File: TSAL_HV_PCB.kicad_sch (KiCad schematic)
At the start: 36 parts, among them J3 Conn_01x03_Socket, J4 Conn_01x03_Socket, K1 SPU01M-12, U1 LM393, U2 4N35, U3 TPS7B88-Q1

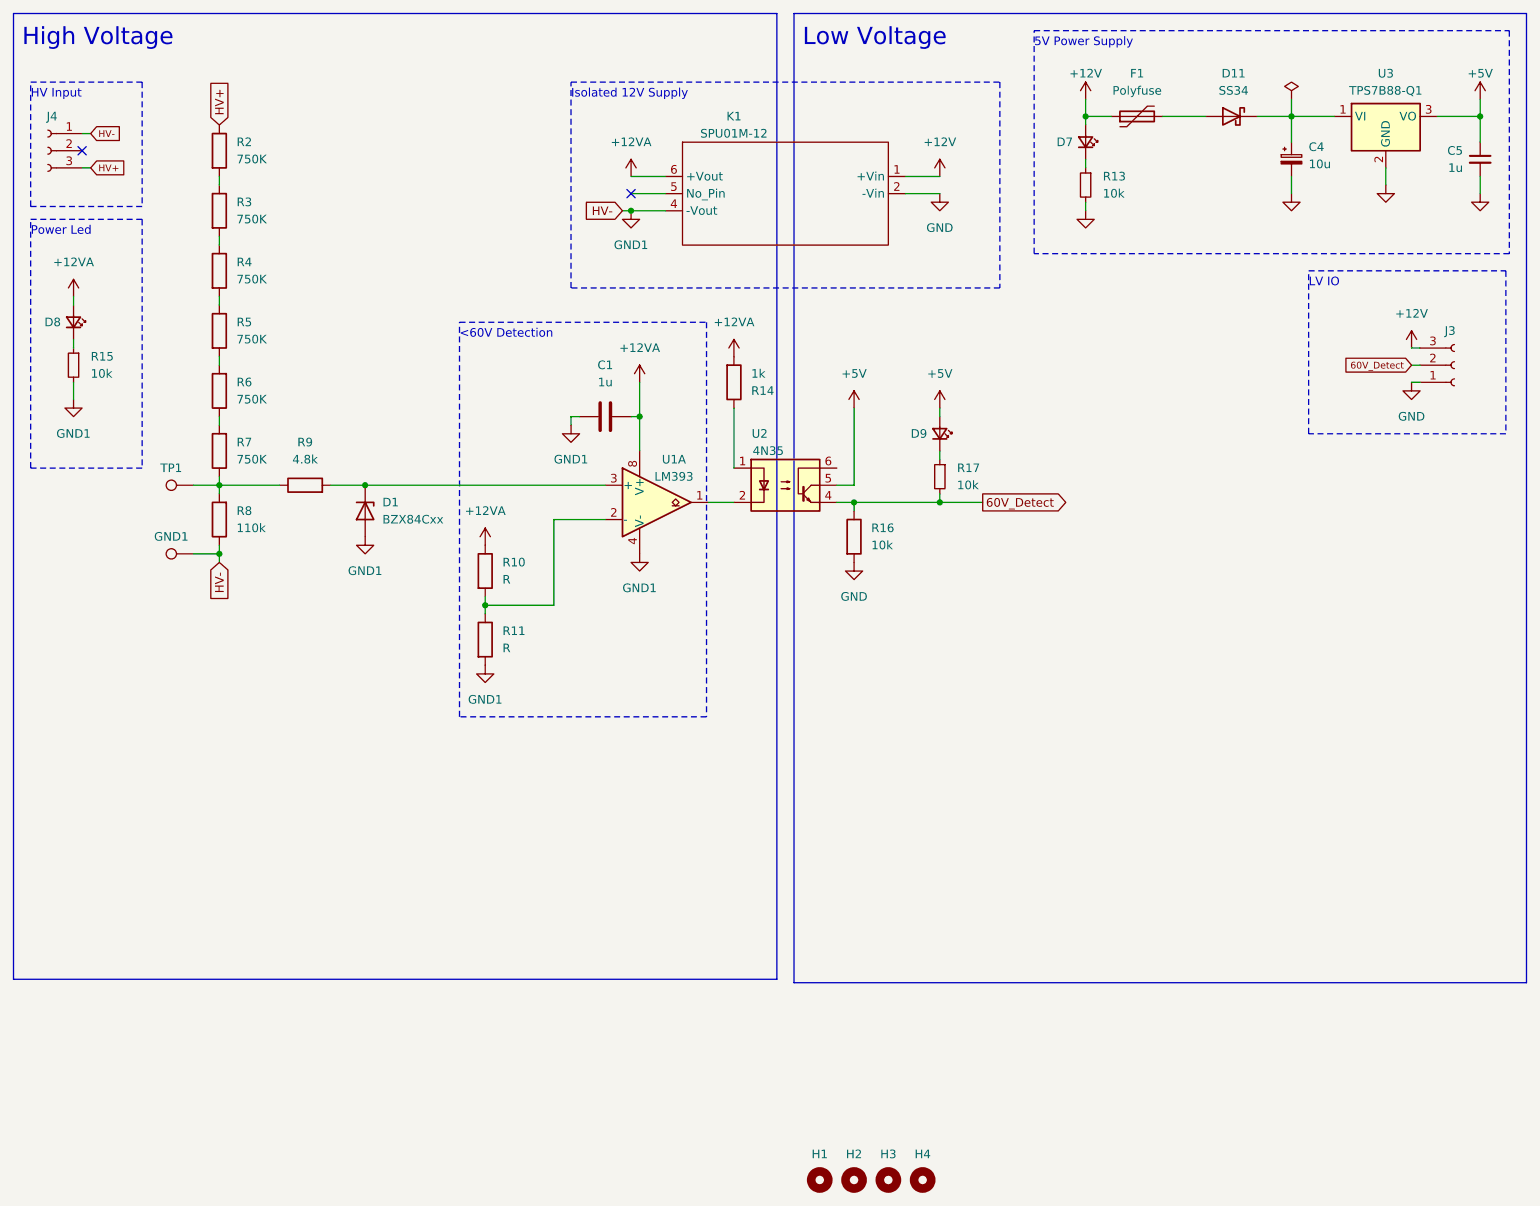
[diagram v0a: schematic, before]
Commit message: Changed LED Indicator, updated footprints
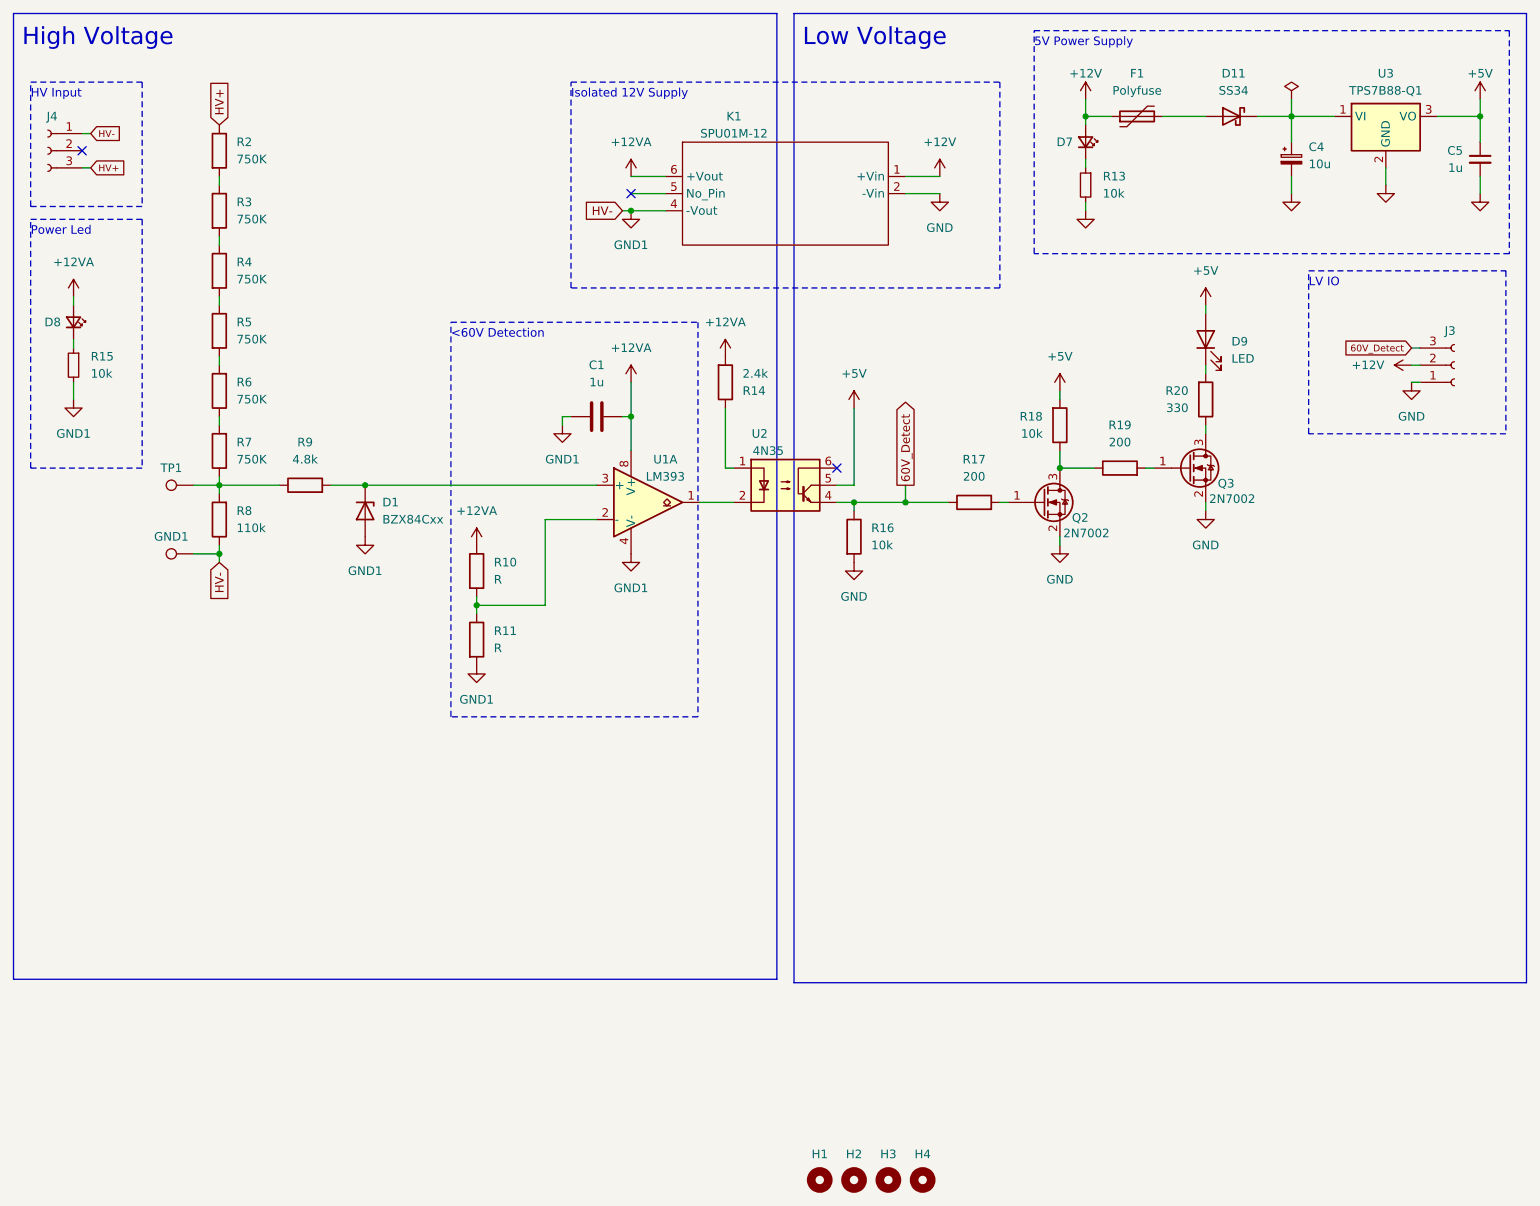
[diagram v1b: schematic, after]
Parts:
- removed D9: LED_Small, LED_SMD:LED_0603_1608Metric, symbol Device:LED_Small
- removed R17: 10k, Resistor_SMD:R_0603_1608Metric, symbol Device:R_Small
- added D9: LED, LED_SMD:LED_0603_1608Metric, symbol Device:LED
- added Q2, Q3: 2N7002, Package_TO_SOT_SMD:SOT-23, symbol Transistor_FET:2N7002
- added R17, R19: 200, Resistor_SMD:R_0603_1608Metric, symbol Device:R
- added R18: 10k, Resistor_SMD:R_0603_1608Metric, symbol Device:R
- added R20: 330, Resistor_SMD:R_0603_1608Metric, symbol Device:R
- J3, J4: footprint MyLibrary:MolexMicrofitPlus1x3 -> yfs:MolexMicrofitPlus1x3
- K1: footprint MyLibrary:SPU01M-12 -> yfs:SPU01M-12
- R14: value 1k -> 2.4k
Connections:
- net +12V: now also J3.2 (Pin_2); no longer J3.3 (Pin_3)
- net +5V: now also D9.2 (A), R18.2
- net 60V_Detect: now also J3.3 (Pin_3), R17.1; no longer J3.2 (Pin_2)
- net GND: now also Q2.2 (S), Q3.2 (S)
- new net: Q2.3 (D), R18.1, R19.1
- new net: Q3.1 (G), R19.2
- new net: Q3.3 (D), R20.1
- new net: Q2.1 (G), R17.2
- new net: D9.1 (K), R20.2
- no-connect marks 2 -> 3
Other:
- moved on the sheet: C1, R10, R11, R14, U1A

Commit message: Changed DC-DC Converter
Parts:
- removed D1: BZX84Cxx, Package_TO_SOT_SMD:SOT-23, symbol Diode:BZX84Cxx
- added D1: BZX384xxxx, Diode_SMD:D_SOD-323, symbol Diode:BZX384xxxx
- D11: value SS34 -> NSR0530HT1G; footprint Diode_SMD:D_SMA -> Diode_SMD:D_SOD-323
- K1: value SPU01M-12 -> SPU01M-5; footprint yfs:SPU01M-12 -> yfs:SPU01M-5
- R14: value 2.4k -> 1.8k
- R15: value 10k -> 1k
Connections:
- net GND1: now also D1.2 (A)
- net at R9.2, U1.3 (+): now also D1.1 (K)
- net +12VA renamed +5VA
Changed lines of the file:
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@@
 	)
 	(junction
-		(at 86.36 87.63)
-		(diameter 0)
-		(color 0 0 0 0)
-	)
-	(junction
 		(at 166.37 90.17)
 		(diameter 0)
@@
 		(color 0 0 0 0)
 	)
+	(junction
+		(at 86.36 87.63)
+		(diameter 0)
+		(color 0 0 0 0)
+	)
 	(no_connect
 		(at 44.45 38.1)
@@
 	(wire
 		(pts
+			(xy 86.36 87.63) (xy 120.65 87.63)
+		)
+		(stroke
+			(width 0)
+			(type default)
+		)
+	)
+	(wire
+		(pts
 			(xy 210.82 90.17) (xy 210.82 91.44)
 		)
@@
 	(wire
 		(pts
-			(xy 86.36 87.63) (xy 120.65 87.63)
-		)
-		(stroke
-			(width 0)
-			(type default)
-		)
-	)
-	(wire
-		(pts
 			(xy 210.82 60.96) (xy 210.82 62.23)
 		)
@@
 	)
 	(symbol
-		(lib_id "Diode:BZX84Cxx")
-		(at 86.36 91.44 270)
-		(unit 1)
-		(exclude_from_sim no)
-		(in_bom yes)
-		(on_board yes)
-		(dnp no)
-		(fields_autoplaced yes)
-		(property "Reference" "D1"
-			(at 88.9 90.17 90)
-			(effects
-				(font
-					(size 1.27 1.27)
-				)
-				(justify left)
-			)
-		)
-		(property "Value" "BZX84Cxx"
-			(at 88.9 92.71 90)
-			(effects
-				(font
-					(size 1.27 1.27)
-				)
-				(justify left)
-			)
-		)
-		(property "Footprint" "Package_TO_SOT_SMD:SOT-23"
-			(at 86.36 91.44 0)
-			(effects
-				(font
-					(size 1.27 1.27)
-				)
-				(hide yes)
-			)
-		)
-		(property "Datasheet" "https://diotec.com/tl_files/diotec/files/pdf/datasheets/bzx84c2v4.pdf"
-			(at 86.36 91.44 0)
-			(effects
-				(font
-					(size 1.27 1.27)
-				)
-				(hide yes)
-			)
-		)
-		(property "Description" ""
-			(at 86.36 91.44 0)
-			(effects
-				(font
-					(size 1.27 1.27)
-				)
-				(hide yes)
-			)
-		)
-		(pin "1"
-		)
-		(pin "2"
-		)
-		(pin "3"
-		)
-		(instances
-			(project "TSAL_HV_PCB"
-				(path "/49aa962b-9fa6-407b-842a-3cf8300a05dc"
-					(reference "D1")
-					(unit 1)
-				)
-			)
-		)
-	)
-	(symbol
 		(lib_id "power:+5V")
 		(at 189.23 73.66 0)
@@
 		(on_board yes)
 		(dnp no)
-		(fields_autoplaced yes)
 		(property "Reference" "#PWR09"
 			(at 125.73 45.72 0)
@@
 			)
 		)
-		(property "Value" "+12VA"
-			(at 125.73 36.83 0)
+		(property "Value" "+5VA"
+			(at 123.19 36.83 0)
 			(effects
 				(font
 					(size 1.27 1.27)
 				)
+				(justify left)
 			)
 		)
@@
 	)
 	(symbol
+		(lib_id "Diode:BZX384xxxx")
+		(at 86.36 91.44 270)
+		(unit 1)
+		(exclude_from_sim no)
+		(in_bom yes)
+		(on_board yes)
+		(dnp no)
+		(fields_autoplaced yes)
+		(property "Reference" "D1"
+			(at 88.9 90.1699 90)
+			(effects
+				(font
+					(size 1.27 1.27)
+				)
+				(justify left)
+			)
+		)
+		(property "Value" "BZX384xxxx"
+			(at 88.9 92.7099 90)
+			(effects
+				(font
+					(size 1.27 1.27)
+				)
+				(justify left)
+			)
+		)
+		(property "Footprint" "Diode_SMD:D_SOD-323"
+			(at 81.915 91.44 0)
+			(effects
+				(font
+					(size 1.27 1.27)
+				)
+				(hide yes)
+			)
+		)
+		(property "Datasheet" "https://www.vishay.com/docs/86474/bzx384.pdf"
+			(at 86.36 91.44 0)
+			(effects
+				(font
+					(size 1.27 1.27)
+				)
+				(hide yes)
+			)
+		)
+		(property "Description" "300mW Zener Diode, SOD-323"
+			(at 86.36 91.44 0)
+			(effects
+				(font
+					(size 1.27 1.27)
+				)
+				(hide yes)
+			)
+		)
+		(pin "2"
+		)
+		(pin "1"
+		)
+		(instances
+			(project "TSAL_HV_PCB"
+				(path "/49aa962b-9fa6-407b-842a-3cf8300a05dc"
+					(reference "D1")
+					(unit 1)
+				)
+			)
+		)
+	)
+	(symbol
 		(lib_id "power:GND")
 		(at 223.52 44.45 0)
@@
 		(on_board yes)
 		(dnp no)
-		(fields_autoplaced yes)
 		(property "Reference" "#PWR011"
 			(at 125.73 76.2 0)
@@
 			)
 		)
-		(property "Value" "+12VA"
-			(at 125.73 67.31 0)
+		(property "Value" "+5VA"
+			(at 123.19 68.58 0)
 			(effects
 				(font
 					(size 1.27 1.27)
 				)
+				(justify left)
 			)
 		)
@@
 			)
 		)
-		(property "Value" "10k"
+		(property "Value" "1k"
 			(at 45.72 71.1199 0)
 			(effects
@@
 			)
 		)
-		(property "Value" "+12VA"
+		(property "Value" "+5VA"
 			(at 43.18 54.61 0)
 			(effects
@@
 			)
 		)
-		(property "Value" "2.4k"
+		(property "Value" "1.8k"
 			(at 142.24 71.12 0)
 			(effects
@@
 			)
 		)
-		(property "Value" "SPU01M-12"
+		(property "Value" "SPU01M-5"
 			(at 140.97 35.56 0)
 			(effects
@@
 			)
 		)
-		(property "Footprint" "yfs:SPU01M-12"
+		(property "Footprint" "yfs:SPU01M-5"
 			(at 137.16 38.1 0)
 			(effects
@@
 			)
 		)
-		(property "Datasheet" ""
+		(property "Datasheet" "https://www.meanwellusa.com/webapp/product/search.aspx?prod=SPU01"
 			(at 137.16 38.1 0)
 			(effects
@@
 			)
 		)
-		(property "Description" ""
+		(property "Description" "Isolated DC/DC Converters - Through Hole 10.8-13.2Vin 5Vout 200mA SIP6 Unreg Iso"
 			(at 138.43 38.1 0)
 			(effects
@@
 			)
 		)
-		(property "Value" "SS34"
+		(property "Value" "NSR0530HT1G"
 			(at 214.9475 29.21 0)
 			(effects
@@
 			)
 		)
-		(property "Footprint" "Diode_SMD:D_SMA"
+		(property "Footprint" "Diode_SMD:D_SOD-323"
 			(at 214.63 37.465 0)
 			(effects
@@
 			)
 		)
-		(property "Datasheet" "https://www.vishay.com/docs/88751/ss32.pdf"
+		(property "Datasheet" "https://www.mouser.co.uk/datasheet/3/101/1/NSR0530H-D.PDF"
 			(at 214.63 33.02 0)
 			(effects
@@
 			)
 		)
-		(property "Description" "40V 3A Schottky Diode, SMA"
+		(property "Description" "Schottky Diodes & Rectifiers 0.5 A 30 V SOD-323 S"
 			(at 214.63 33.02 0)
 			(effects
@@
 			)
 		)
-		(property "Value" "+12VA"
+		(property "Value" "+5VA"
 			(at 102.87 91.44 0)
 			(effects
@@
 		(on_board yes)
 		(dnp no)
-		(fields_autoplaced yes)
 		(property "Reference" "#PWR013"
 			(at 139.7 72.39 0)
@@
 			)
 		)
-		(property "Value" "+12VA"
-			(at 139.7 63.5 0)
+		(property "Value" "+5VA"
+			(at 138.43 63.5 0)
 			(effects
 				(font
 					(size 1.27 1.27)
 				)
+				(justify left)
 			)
 		)

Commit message: Polyfuse for DC-DC supply
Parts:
- added F2: 500mA, Resistor_SMD:R_0805_2012Metric, symbol Device:Polyfuse
- F1: value Polyfuse -> 100mA
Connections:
- net +12V: now also F2.2; no longer K1.1 (+Vin)
- new net: F2.1, K1.1 (+Vin)
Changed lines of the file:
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@@
 	(rectangle
 		(start 116.84 27.94)
-		(end 180.34 58.42)
+		(end 182.88 58.42)
 		(stroke
 			(width 0)
@@
 	(wire
 		(pts
-			(xy 166.37 41.91) (xy 171.45 41.91)
+			(xy 201.93 85.09) (xy 203.2 85.09)
 		)
 		(stroke
@@
 	(wire
 		(pts
-			(xy 201.93 85.09) (xy 203.2 85.09)
+			(xy 241.3 72.39) (xy 242.57 72.39)
 		)
 		(stroke
@@
 	(wire
 		(pts
-			(xy 241.3 72.39) (xy 242.57 72.39)
+			(xy 193.04 30.48) (xy 193.04 33.02)
 		)
 		(stroke
@@
 	(wire
 		(pts
-			(xy 193.04 30.48) (xy 193.04 33.02)
+			(xy 172.72 41.91) (xy 166.37 41.91)
 		)
 		(stroke
@@
 	(symbol
 		(lib_id "power:+12V")
-		(at 171.45 41.91 0)
+		(at 172.72 34.29 0)
 		(unit 1)
 		(exclude_from_sim no)
@@
 		(fields_autoplaced yes)
 		(property "Reference" "#PWR019"
-			(at 171.45 45.72 0)
+			(at 172.72 38.1 0)
 			(effects
 				(font
@@
 		)
 		(property "Value" "+12V"
-			(at 171.45 36.83 0)
+			(at 172.72 29.21 0)
 			(effects
 				(font
@@
 		)
 		(property "Footprint" ""
-			(at 171.45 41.91 0)
+			(at 172.72 34.29 0)
 			(effects
 				(font
@@
 		)
 		(property "Datasheet" ""
-			(at 171.45 41.91 0)
+			(at 172.72 34.29 0)
 			(effects
 				(font
@@
 		)
 		(property "Description" ""
-			(at 171.45 41.91 0)
+			(at 172.72 34.29 0)
 			(effects
 				(font
@@
 			)
 		)
-		(property "Value" "Polyfuse"
+		(property "Value" "100mA"
 			(at 200.66 29.21 90)
 			(effects
@@
 					(unit 1)
 				)
+			)
+		)
+	)
+	(symbol
+		(lib_id "Device:Polyfuse")
+		(at 172.72 38.1 180)
+		(unit 1)
+		(exclude_from_sim no)
+		(in_bom yes)
+		(on_board yes)
+		(dnp no)
+		(fields_autoplaced yes)
+		(property "Reference" "F2"
+			(at 175.26 36.8299 0)
+			(effects
+				(font
+					(size 1.27 1.27)
+				)
+				(justify right)
+			)
+		)
+		(property "Value" "500mA"
+			(at 175.26 39.3699 0)
+			(effects
+				(font
+					(size 1.27 1.27)
+				)
+				(justify right)
+			)
+		)
+		(property "Footprint" "Resistor_SMD:R_0805_2012Metric"
+			(at 171.45 33.02 0)
+			(effects
+				(font
+					(size 1.27 1.27)
+				)
+				(justify left)
+				(hide yes)
+			)
+		)
+		(property "Datasheet" "~"
+			(at 172.72 38.1 0)
+			(effects
+				(font
+					(size 1.27 1.27)
+				)
+				(hide yes)
+			)
+		)
+		(property "Description" "Resettable fuse, polymeric positive temperature coefficient"
+			(at 172.72 38.1 0)
+			(effects
+				(font
+					(size 1.27 1.27)
+				)
+				(hide yes)
+			)
+		)
+		(pin "2"
+		)
+		(pin "1"
+		)
+		(instances
+			(project "TSAL_HV_PCB"
+				(path "/49aa962b-9fa6-407b-842a-3cf8300a05dc"
+					(reference "F2")
+					(unit 1)
+				)
